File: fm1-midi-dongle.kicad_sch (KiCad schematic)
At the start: 29 parts, among them J1 911-321B2028S10100, J2 TYPE-C-31-M-12, J3 PJ-320D, J4 PJ-320D, U1 CH32X035G8U6, U2 XC6206P332MR, U3 SY6280AAC, U4 H11L1SM, U5 SN74LVC1G3157

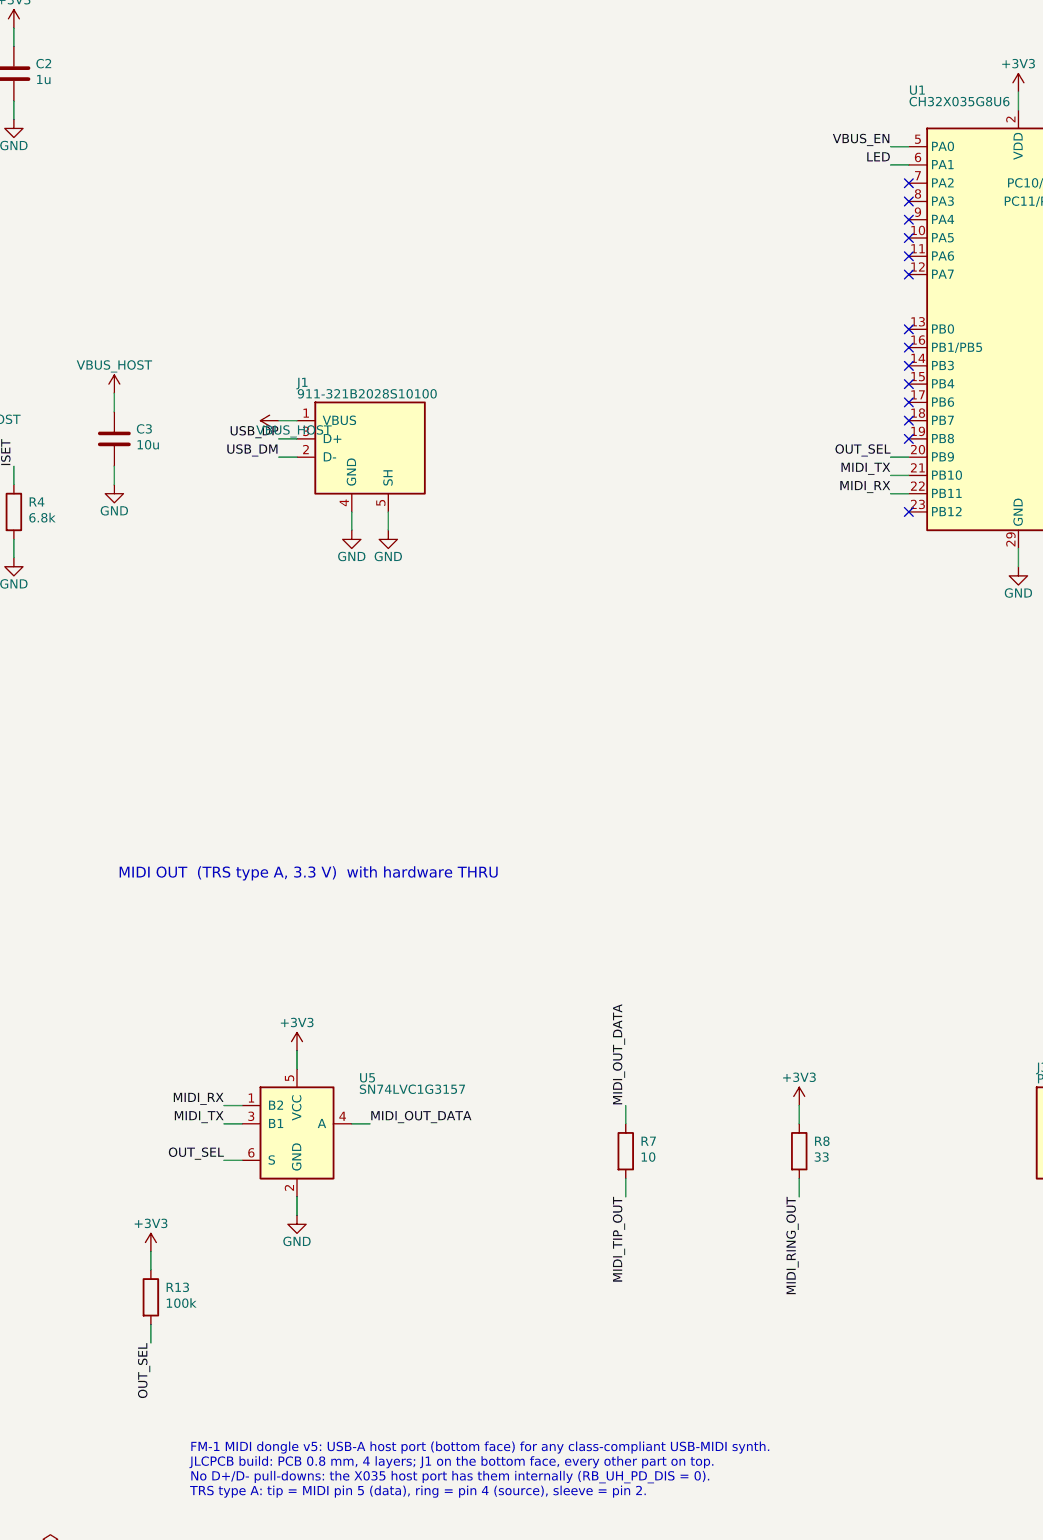
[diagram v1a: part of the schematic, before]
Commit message: v6: flat-slab layout, hand-routed, slab case
Owner rejected the v5 S-profile case (can't lie flat on a desk) and chose a
re-placed board in a uniform 12.2 mm slab.

- Board (still 20 x 37.7 mm): tall parts on top (USB-A J1 now on top, USB-C
  J2 on the right edge, jacks, opto, THRU switch, LED); parts <= 1.3 mm on
  the bottom (MCU, LDO, SY6280, caps, SDI pads).
- Pins: VBUS_EN -> PA3 (pin 8), LED -> PB12 (pin 23); U5 B1 = RX, B2 = TX,
  R13 back to a pull-down (PB9 HIGH = MCU TX, default hardware THRU).
- Routing (tools/route.py, hand-written polylines): +5V_IN as an island in
  In2; DRC 0 unconnected / 0 clearance, 0 loops, style clean. Open for
  owner sign-off: VDD 0.2 mm neck, one 0.6/0.3 +5V via, 0.8 mm designators.
- tools/silk.py is face-aware (outlines, designators and labels on each
  part's own face, back text mirrored); per-face net renders.
- case/: rounded slab 22.8 x 41.0 x 12.2 mm, flat top and bottom, snap fit,
  USB-A / USB-C dishes, flush jacks, LED light pipe; check_fit 0 collisions.
- DESIGN.md v6 section and firmware pin changes; BOM notes.

Co-Authored-By: Claude Opus 5.5 <noreply@anthropic.com>
Claude-Session: https://claude.ai/code/session_01Dtfv3zuhZTs975LiSXznFQ
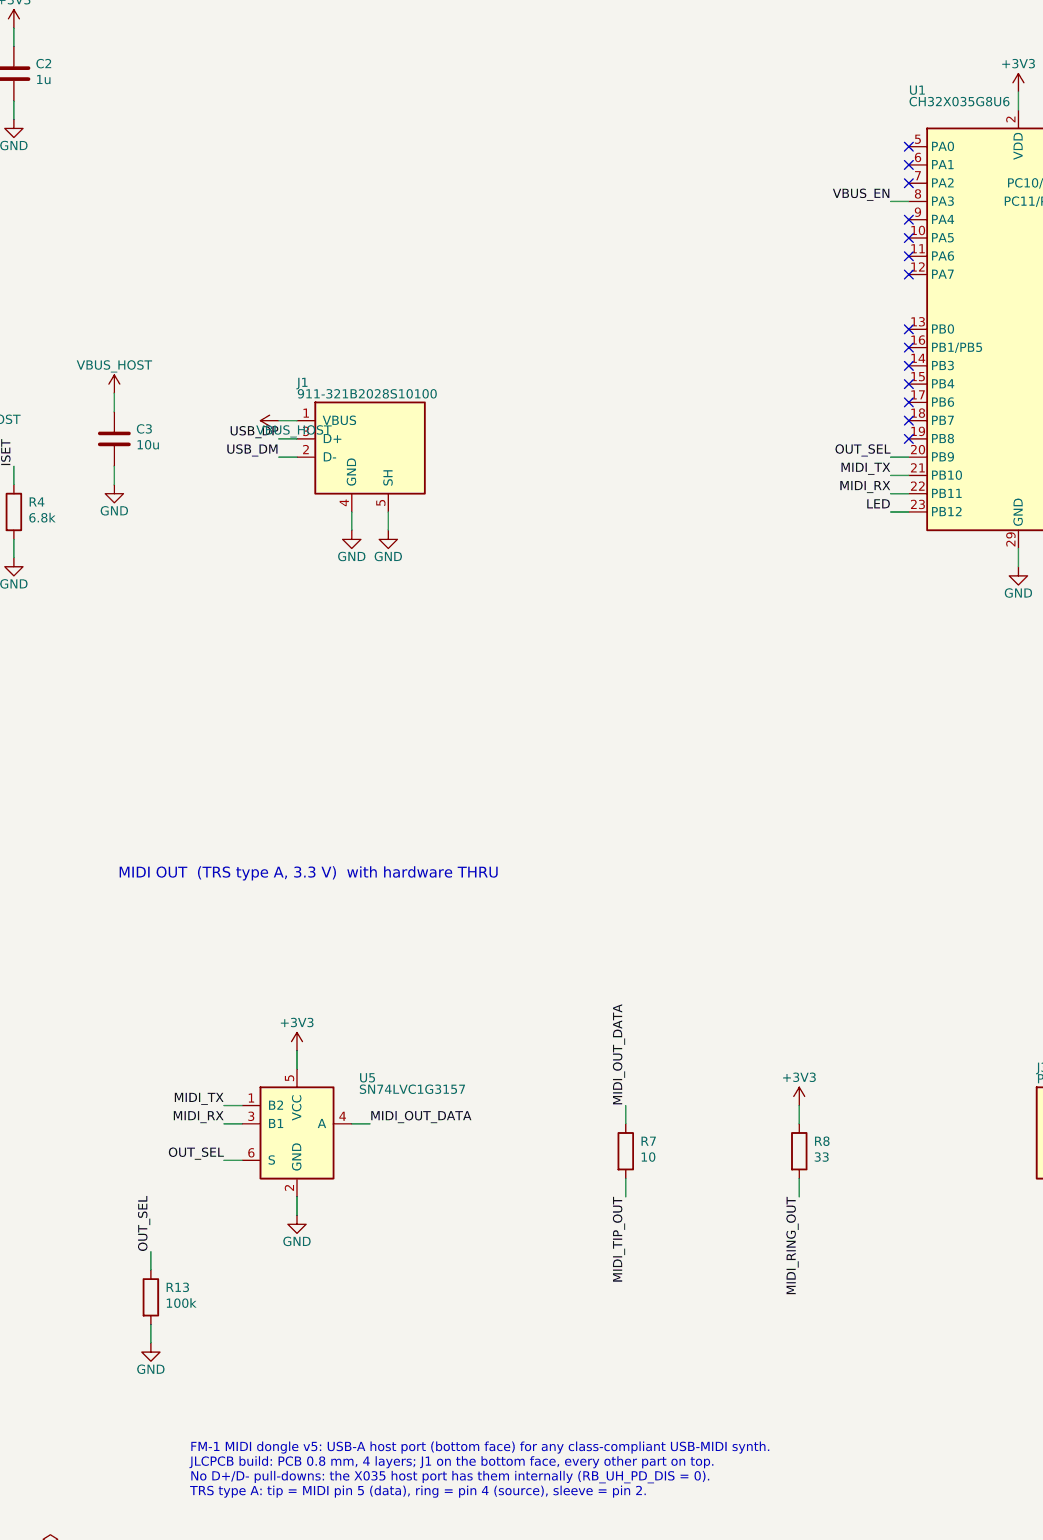
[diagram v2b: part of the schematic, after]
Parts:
- R13: Note OUT_SEL pull-up: default high = hardware THRU until firmwar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 -> OUT_SEL pull-down: default low = hardware THRU until firmwa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
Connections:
- net +3V3: no longer R13.1
- net GND: now also R13.2
- net LED: now also U1.23 (PB12); no longer U1.6 (PA1)
- net MIDI_RX: now also U5.3 (B1); no longer U5.1 (B2)
- net MIDI_TX: now also U5.1 (B2); no longer U5.3 (B1)
- net OUT_SEL: now also R13.1; no longer R13.2
- net VBUS_EN: now also U1.8 (PA3); no longer U1.5 (PA0)
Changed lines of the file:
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@@
 	(no_connect (at 345.44 59.69))
 	(no_connect (at 345.44 62.23))
+	(no_connect (at 314.96 59.69))
+	(no_connect (at 314.96 62.23))
 	(no_connect (at 314.96 64.77))
-	(no_connect (at 314.96 67.31))
 	(no_connect (at 314.96 69.85))
 	(no_connect (at 314.96 72.39))
@@
 	(no_connect (at 314.96 97.79))
 	(no_connect (at 314.96 100.33))
-	(no_connect (at 314.96 110.49))
 	(no_connect (at 345.44 77.47))
 	(no_connect (at 345.44 69.85))
@@
 		(instances (project "fm1-midi-dongle" (path "/7f2a1c4e-0b3d-4c1a-9e8f-5a6b7c8d9e0f" (reference "#PWR023") (unit 1))))
 	)
-	(wire (pts (xy 314.96 59.69) (xy 312.42 59.69)) (stroke (width 0) (type default)))
-	(label "VBUS_EN" (at 312.42 59.69 180) (effects (font (size 1.27 1.27)) (justify right bottom)))
-	(wire (pts (xy 314.96 62.23) (xy 312.42 62.23)) (stroke (width 0) (type default)))
-	(label "LED" (at 312.42 62.23 180) (effects (font (size 1.27 1.27)) (justify right bottom)))
+	(wire (pts (xy 314.96 67.31) (xy 312.42 67.31)) (stroke (width 0) (type default)))
+	(label "VBUS_EN" (at 312.42 67.31 180) (effects (font (size 1.27 1.27)) (justify right bottom)))
 	(wire (pts (xy 314.96 102.87) (xy 312.42 102.87)) (stroke (width 0) (type default)))
 	(label "OUT_SEL" (at 312.42 102.87 180) (effects (font (size 1.27 1.27)) (justify right bottom)))
@@
 	(wire (pts (xy 314.96 107.95) (xy 312.42 107.95)) (stroke (width 0) (type default)))
 	(label "MIDI_RX" (at 312.42 107.95 180) (effects (font (size 1.27 1.27)) (justify right bottom)))
+	(wire (pts (xy 314.96 110.49) (xy 312.42 110.49)) (stroke (width 0) (type default)))
+	(label "LED" (at 312.42 110.49 180) (effects (font (size 1.27 1.27)) (justify right bottom)))
 	(wire (pts (xy 345.44 74.93) (xy 347.98 74.93)) (stroke (width 0) (type default)))
 	(label "SDI_DIO" (at 347.98 74.93 0) (effects (font (size 1.27 1.27)) (justify left bottom)))
@@
 	(text "MIDI OUT  (TRS type A, 3.3 V)  with hardware THRU" (exclude_from_sim no) (at 205 160 0) (effects (font (size 1.5 1.5)) (justify left top)))
 	(wire (pts (xy 222.25 193.04) (xy 219.71 193.04)) (stroke (width 0) (type default)))
-	(label "MIDI_RX" (at 219.71 193.04 180) (effects (font (size 1.27 1.27)) (justify right bottom)))
+	(label "MIDI_TX" (at 219.71 193.04 180) (effects (font (size 1.27 1.27)) (justify right bottom)))
 	(wire (pts (xy 229.87 205.74) (xy 229.87 208.28)) (stroke (width 0) (type default)))
 	(symbol (lib_id "power:GND") (at 229.87 208.28 0) (unit 1) (exclude_from_sim no) (in_bom no) (on_board yes) (dnp no)
@@
 	)
 	(wire (pts (xy 222.25 195.58) (xy 219.71 195.58)) (stroke (width 0) (type default)))
-	(label "MIDI_TX" (at 219.71 195.58 180) (effects (font (size 1.27 1.27)) (justify right bottom)))
+	(label "MIDI_RX" (at 219.71 195.58 180) (effects (font (size 1.27 1.27)) (justify right bottom)))
 	(wire (pts (xy 237.49 195.58) (xy 240.03 195.58)) (stroke (width 0) (type default)))
 	(label "MIDI_OUT_DATA" (at 240.03 195.58 0) (effects (font (size 1.27 1.27)) (justify left bottom)))
@@
 	)
 	(wire (pts (xy 209.55 215.9) (xy 209.55 213.36)) (stroke (width 0) (type default)))
-	(symbol (lib_id "power:+3V3") (at 209.55 213.36 0) (unit 1) (exclude_from_sim no) (in_bom no) (on_board yes) (dnp no)
-		(property "Reference" "#PWR034" (at 209.55 213.36 0) (effects (font (size 1.27 1.27)) (hide yes)))
-		(property "Value" "+3V3" (at 209.55 210.22 0) (effects (font (size 1.27 1.27)) (justify bottom)))
-		(property "Footprint" "" (at 209.55 213.36 0) (effects (font (size 1.27 1.27)) (hide yes)))
-		(property "Datasheet" "" (at 209.55 213.36 0) (effects (font (size 1.27 1.27)) (hide yes)))
+	(label "OUT_SEL" (at 209.55 213.36 90) (effects (font (size 1.27 1.27)) (justify left bottom)))
+	(wire (pts (xy 209.55 223.52) (xy 209.55 226.06)) (stroke (width 0) (type default)))
+	(symbol (lib_id "power:GND") (at 209.55 226.06 0) (unit 1) (exclude_from_sim no) (in_bom no) (on_board yes) (dnp no)
+		(property "Reference" "#PWR034" (at 209.55 226.06 0) (effects (font (size 1.27 1.27)) (hide yes)))
+		(property "Value" "GND" (at 209.55 230.5 0) (effects (font (size 1.27 1.27)) (justify bottom)))
+		(property "Footprint" "" (at 209.55 226.06 0) (effects (font (size 1.27 1.27)) (hide yes)))
+		(property "Datasheet" "" (at 209.55 226.06 0) (effects (font (size 1.27 1.27)) (hide yes)))
 		(pin "1")
 		(instances (project "fm1-midi-dongle" (path "/7f2a1c4e-0b3d-4c1a-9e8f-5a6b7c8d9e0f" (reference "#PWR034") (unit 1))))
 	)
-	(wire (pts (xy 209.55 223.52) (xy 209.55 226.06)) (stroke (width 0) (type default)))
-	(label "OUT_SEL" (at 209.55 226.06 270) (effects (font (size 1.27 1.27)) (justify right bottom)))
 	(symbol (lib_id "Device:R") (at 209.55 219.71 0) (unit 1) (exclude_from_sim no) (in_bom yes) (on_board yes) (dnp no)
 		(property "Reference" "R13" (at 211.566 219.11 0) (effects (font (size 1.27 1.27)) (justify left bottom)))
@@
 		(property "LCSC#" "C25803" (at 209.55 219.71 0) (effects (font (size 1.27 1.27)) (justify left bottom) (hide yes)))
 		(property "MPN" "0603WAF1003T5E" (at 209.55 219.71 0) (effects (font (size 1.27 1.27)) (justify left bottom) (hide yes)))
-		(property "Note" "OUT_SEL pull-up: default high = hardware THRU until firmware drives PB9 low" (at 209.55 219.71 0) (effects (font (size 1.27 1.27)) (justify left bottom) (hide yes)))
-		(pin "1")
-		(pin "2")
+		(property "Note" "OUT_SEL pull-down: default low = hardware THRU until firmware drives PB9 high" (at 209.55 219.71 0) (effects (font (size 1.27 1.27)) (justify left bottom) (hide yes)))
+		(pin "1")
+		(pin "2")
